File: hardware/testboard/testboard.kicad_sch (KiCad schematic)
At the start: 0 parts

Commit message: work on testboard, move 3d models
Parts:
- added C19: 100nF, symbol Device:C
- added U5: 74LVC1G04, symbol 74xGxx:74LVC1G04
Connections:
- new net +5V: C19.1, U5.5 (VCC)
- new net GND: C19.2, U5.3 (GND)
- new net R/~{W}: U5.2
- new net ~{R}/W: U5.4
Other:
- added sheet Clock (clock.kicad_sch)
- added sheet FPGA (fpga.kicad_sch)
- added sheet IO (io.kicad_sch)
- added sheet Power (power.kicad_sch)
- added sheet Resizer (resizer.kicad_sch)
- added sheet SRAM (sram.kicad_sch)
- sheet CPU ports: added A[0..31], BCLK, D[0..31], PCLK, R/~{W}, SIZ[0..1], TM[0..2], TT[0..1], ~{AVEC}, ~{IPL[0..2]}, ~{RSTI}, ~{RSTO}, ~{TA}, ~{TCI}/~{TBI}, ~{TEA}, ~{TIP}, ~{TS}; removed none

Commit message: work on testboard
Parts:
- removed C19: 100nF, symbol Device:C
- removed U5: 74LVC1G04, symbol 74xGxx:74LVC1G04
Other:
- sheet CPU ports: added ~{R}/W, ~{TBI}, ~{TCI}; removed ~{TCI}/~{TBI}

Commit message: root mostly finished
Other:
- sheet FPGA ports: added D[0..31], IPL[0..2], R/~{W}, SIZ[0..1], TM[0..2], TT[0..1], ~{COM_IACK}, ~{COM_IRQ}, ~{TA}, ~{TBI}, ~{TCI}, ~{TEA}, ~{TIP}, ~{TS}; removed PA[0..1], PD[24..31]

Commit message: work on testboard
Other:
- sheet FPGA ports: added ~{IPL[0..2]}; removed IPL[0..2]
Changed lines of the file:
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@@
-      (effects (font (size 1.27 1.27)) (justify left))
-    )
-    (pin "IPL[0..2]" output (at 137.16 96.52 180)
       (effects (font (size 1.27 1.27)) (justify left))
     )
@@
       (effects (font (size 1.27 1.27)) (justify right))
     )
+    (pin "~{IPL[0..2]}" output (at 137.16 96.52 180)
+      (effects (font (size 1.27 1.27)) (justify left))
+    )
     (instances

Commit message: simpleboard nearly complete
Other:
- added sheet Reset (reset.kicad_sch)
- sheet FPGA ports: added ~{FPGA_RDY}, ~{RST}; removed none
- sheet Power ports: added none; removed PWR_GOOD
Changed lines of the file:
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@@
+    (stroke (width 0) (type default))
+  )
+  (wire (pts (xy 124.46 124.46) (xy 137.16 124.46))
     (stroke (width 0) (type default))
   )
@@
     (stroke (width 0) (type default))
   )
+  (wire (pts (xy 220.98 106.68) (xy 233.68 106.68))
+    (stroke (width 0) (type default))
+  )
   (wire (pts (xy 48.26 142.24) (xy 58.42 142.24))
     (stroke (width 0) (type default))
   )
+  (wire (pts (xy 124.46 45.72) (xy 137.16 45.72))
+    (stroke (width 0) (type default))
+  )
   (wire (pts (xy 83.82 121.92) (xy 96.52 121.92))
     (stroke (width 0) (type default))
@@
     (stroke (width 0) (type default))
   )
+  (wire (pts (xy 91.44 30.48) (xy 101.6 30.48))
+    (stroke (width 0) (type default))
+  )
   (bus (pts (xy 124.46 88.9) (xy 137.16 88.9))
     (stroke (width 0) (type default))
@@
     (stroke (width 0) (type default))
   )
+  (wire (pts (xy 91.44 27.94) (xy 101.6 27.94))
+    (stroke (width 0) (type default))
+  )
   (wire (pts (xy 27.94 25.4) (xy 38.1 25.4))
     (stroke (width 0) (type default))
@@
     (stroke (width 0) (type default))
   )
+  (wire (pts (xy 48.26 162.56) (xy 60.96 162.56))
+    (stroke (width 0) (type default))
+  )
   (bus (pts (xy 101.6 22.86) (xy 91.44 22.86))
     (stroke (width 0) (type default))
@@
     (stroke (width 0) (type default))
   )
+  (wire (pts (xy 60.96 160.02) (xy 48.26 160.02))
+    (stroke (width 0) (type default))
+  )
   (bus (pts (xy 101.6 45.72) (xy 91.44 45.72))
     (stroke (width 0) (type default))
@@
     (stroke (width 0) (type default))
   )
+  (wire (pts (xy 96.52 160.02) (xy 83.82 160.02))
+    (stroke (width 0) (type default))
+  )
   (wire (pts (xy 91.44 83.82) (xy 101.6 83.82))
     (stroke (width 0) (type default))
@@
     (effects (font (size 1.27 1.27)) (justify right bottom))
   )
+  (label "~{SW_RST}" (at 101.6 30.48 180) (fields_autoplaced)
+    (effects (font (size 1.27 1.27)) (justify right bottom))
+  )
   (label "~{AVEC}" (at 101.6 83.82 180) (fields_autoplaced)
     (effects (font (size 1.27 1.27)) (justify right bottom))
   )
+  (label "~{FPGA_RDY}" (at 124.46 124.46 0) (fields_autoplaced)
+    (effects (font (size 1.27 1.27)) (justify left bottom))
+  )
   (label "~{DSACK[0..1]}" (at 96.52 129.54 180) (fields_autoplaced)
     (effects (font (size 1.27 1.27)) (justify right bottom))
@@
     (effects (font (size 1.27 1.27)) (justify right bottom))
   )
+  (label "~{RST}" (at 101.6 27.94 180) (fields_autoplaced)
+    (effects (font (size 1.27 1.27)) (justify right bottom))
+  )
+  (label "~{SW_RST}" (at 48.26 160.02 0) (fields_autoplaced)
+    (effects (font (size 1.27 1.27)) (justify left bottom))
+  )
   (label "~{RAM_CS}" (at 200.66 53.34 180) (fields_autoplaced)
     (effects (font (size 1.27 1.27)) (justify right bottom))
@@
     (effects (font (size 1.27 1.27)) (justify left bottom))
   )
+  (label "~{RST}" (at 124.46 45.72 0) (fields_autoplaced)
+    (effects (font (size 1.27 1.27)) (justify left bottom))
+  )
   (label "~{SWE}" (at 220.98 119.38 0) (fields_autoplaced)
     (effects (font (size 1.27 1.27)) (justify left bottom))
@@
     (effects (font (size 1.27 1.27)) (justify right bottom))
   )
+  (label "~{RST}" (at 96.52 160.02 180) (fields_autoplaced)
+    (effects (font (size 1.27 1.27)) (justify right bottom))
+  )
   (label "PA[0..1]" (at 96.52 111.76 180) (fields_autoplaced)
     (effects (font (size 1.27 1.27)) (justify right bottom))
@@
     (effects (font (size 1.27 1.27)) (justify right bottom))
   )
+  (label "~{RST}" (at 220.98 106.68 0) (fields_autoplaced)
+    (effects (font (size 1.27 1.27)) (justify left bottom))
+  )
   (label "TM[0..2]" (at 124.46 93.98 0) (fields_autoplaced)
     (effects (font (size 1.27 1.27)) (justify left bottom))
@@
   )
   (label "A[2..19]" (at 220.98 43.18 0) (fields_autoplaced)
+    (effects (font (size 1.27 1.27)) (justify left bottom))
+  )
+  (label "~{FPGA_RDY}" (at 48.26 162.56 0) (fields_autoplaced)
     (effects (font (size 1.27 1.27)) (justify left bottom))
   )
@@
     )
   )
-  (sheet (at 119.38 154.94) (size 27.94 25.4) (fields_autoplaced)
+  (sheet (at 22.86 180.34) (size 17.78 7.62) (fields_autoplaced)
     (stroke (width 0.1524) (type solid))
     (fill (color 0 0 0 0.0000))
-    (property "Sheetname" "Power" (at 119.38 154.2284 0)
+    (property "Sheetname" "Power" (at 22.86 179.6284 0)
       (effects (font (size 1.27 1.27)) (justify left bottom))
     )
-    (property "Sheetfile" "power.kicad_sch" (at 119.38 180.9246 0)
+    (property "Sheetfile" "power.kicad_sch" (at 22.86 188.5446 0)
       (effects (font (size 1.27 1.27)) (justify left top))
-    )
-    (pin "PWR_GOOD" output (at 147.32 175.26 0)
-      (effects (font (size 1.27 1.27)) (justify right))
     )
     (instances
@@
     )
   )
-  (sheet (at 137.16 48.26) (size 50.8 73.66) (fields_autoplaced)
+  (sheet (at 137.16 43.18) (size 50.8 83.82) (fields_autoplaced)
     (stroke (width 0.1524) (type solid))
     (fill (color 0 0 0 0.0000))
-    (property "Sheetname" "FPGA" (at 137.16 47.5484 0)
+    (property "Sheetname" "FPGA" (at 137.16 42.4684 0)
       (effects (font (size 1.27 1.27)) (justify left bottom))
     )
-    (property "Sheetfile" "fpga.kicad_sch" (at 137.16 122.5046 0)
+    (property "Sheetfile" "fpga.kicad_sch" (at 137.16 127.5846 0)
       (effects (font (size 1.27 1.27)) (justify left top))
     )
@@
     )
     (pin "~{IPL[0..2]}" output (at 137.16 96.52 180)
+      (effects (font (size 1.27 1.27)) (justify left))
+    )
+    (pin "~{FPGA_RDY}" output (at 137.16 124.46 180)
+      (effects (font (size 1.27 1.27)) (justify left))
+    )
+    (pin "~{RST}" input (at 137.16 45.72 180)
       (effects (font (size 1.27 1.27)) (justify left))
     )
@@
       )
     )
+  )
+  (sheet (at 60.96 157.48) (size 22.86 12.7) (fields_autoplaced)
+    (stroke (width 0.1524) (type solid))
+    (fill (color 0 0 0 0.0000))
+    (property "Sheetname" "Reset" (at 60.96 156.7684 0)
+      (effects (font (size 1.27 1.27)) (justify left bottom))
+    )
+    (property "Sheetfile" "reset.kicad_sch" (at 60.96 170.7646 0)
+      (effects (font (size 1.27 1.27)) (justify left top))
+    )
+    (pin "~{RST}" output (at 83.82 160.02 0)
+      (effects (font (size 1.27 1.27)) (justify right))
+    )
+    (pin "SW_RST" input (at 60.96 160.02 180)
+      (effects (font (size 1.27 1.27)) (justify left))
+    )
+    (pin "~{FPGA_RDY}" input (at 60.96 162.56 180)
+      (effects (font (size 1.27 1.27)) (justify left))
+    )
+    (instances
+      (project "testboard"
+        (path "/a1ce156a-fb78-423b-b05a-d07384e5c8a7" (page "12"))
+      )
+    )

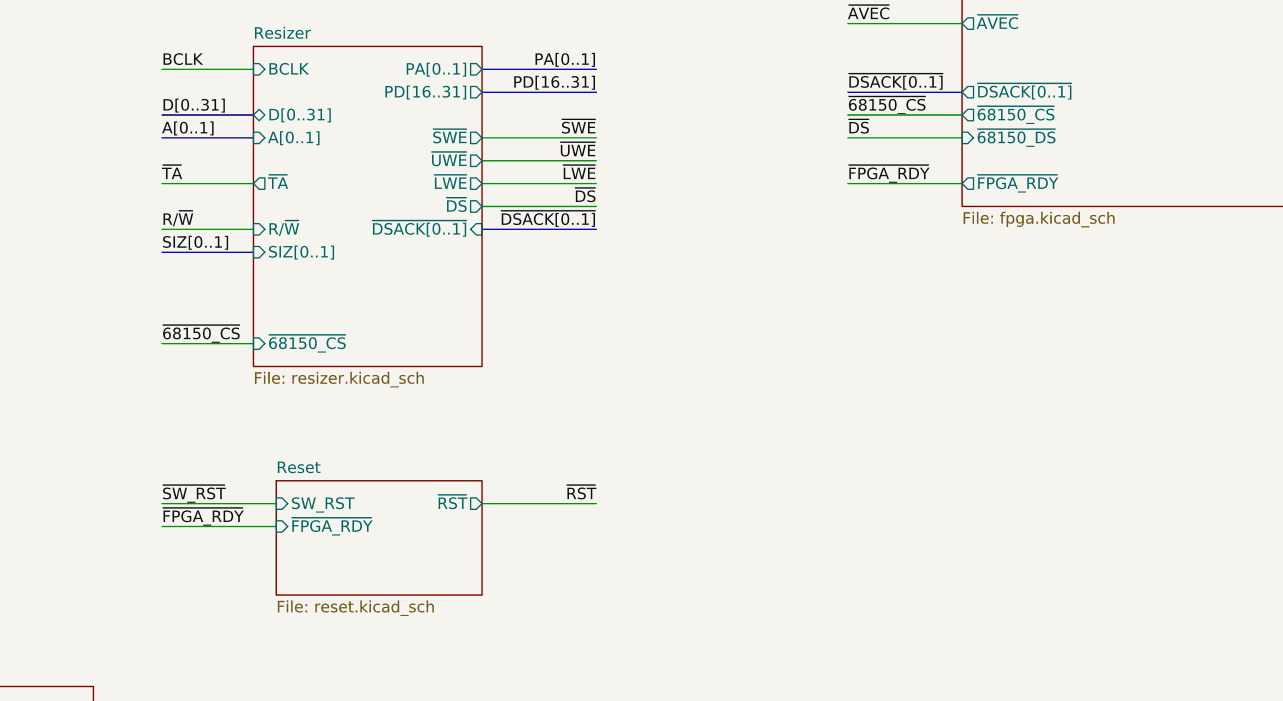
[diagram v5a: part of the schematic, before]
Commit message: testboard - schematic and route done
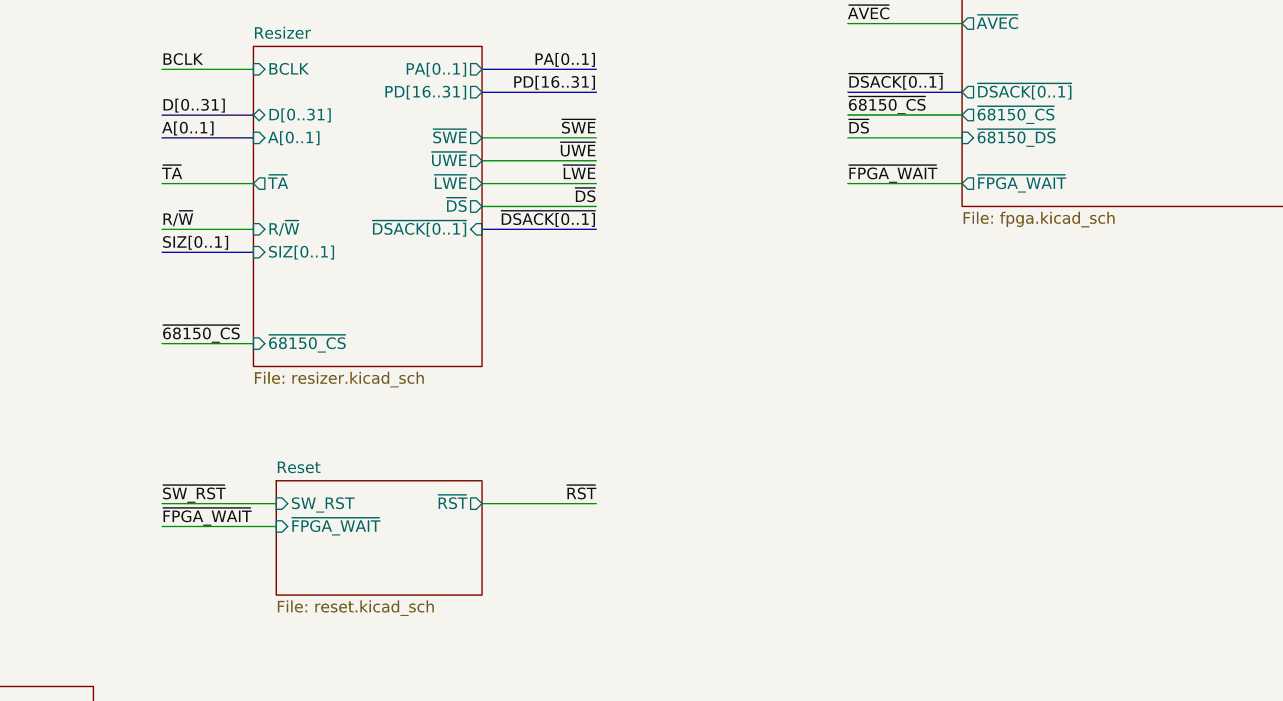
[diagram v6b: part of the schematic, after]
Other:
- sheet FPGA ports: added ~{FPGA_WAIT}; removed ~{FPGA_RDY}
- sheet Reset ports: added ~{FPGA_WAIT}; removed ~{FPGA_RDY}
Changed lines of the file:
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@@
     (effects (font (size 1.27 1.27)) (justify right bottom))
   )
-  (label "~{FPGA_RDY}" (at 124.46 124.46 0) (fields_autoplaced)
+  (label "~{FPGA_WAIT}" (at 124.46 124.46 0) (fields_autoplaced)
     (effects (font (size 1.27 1.27)) (justify left bottom))
   )
@@
     (effects (font (size 1.27 1.27)) (justify left bottom))
   )
-  (label "~{FPGA_RDY}" (at 48.26 162.56 0) (fields_autoplaced)
+  (label "~{FPGA_WAIT}" (at 48.26 162.56 0) (fields_autoplaced)
     (effects (font (size 1.27 1.27)) (justify left bottom))
   )
@@
       (effects (font (size 1.27 1.27)) (justify left))
     )
-    (pin "~{FPGA_RDY}" output (at 137.16 124.46 180)
+    (pin "~{FPGA_WAIT}" output (at 137.16 124.46 180)
       (effects (font (size 1.27 1.27)) (justify left))
     )
@@
       (effects (font (size 1.27 1.27)) (justify left))
     )
-    (pin "~{FPGA_RDY}" input (at 60.96 162.56 180)
-      (effects (font (size 1.27 1.27)) (justify left))
-    )
+    (pin "~{FPGA_WAIT}" input (at 60.96 162.56 180)
+      (effects (font (size 1.27 1.27)) (justify left))
+    )

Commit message: Gerbers published, board out for production!
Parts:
- added H1, H2, H3: MountingHole, MountingHole:MountingHole_3.2mm_M3, symbol Mechanical:MountingHole
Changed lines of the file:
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@@
     (effects (font (size 1.27 1.27)) (justify left bottom))
+  )
+  (symbol (lib_id "Mechanical:MountingHole") (at 142.24 180.34 0) (unit 1)
+    (in_bom yes) (on_board yes) (dnp no) (fields_autoplaced)
+    (property "Reference" "H2" (at 144.78 179.07 0)
+      (effects (font (size 1.27 1.27)) (justify left))
+    )
+    (property "Value" "MountingHole" (at 144.78 181.61 0)
+      (effects (font (size 1.27 1.27)) (justify left))
+    )
+    (property "Footprint" "MountingHole:MountingHole_3.2mm_M3" (at 142.24 180.34 0)
+      (effects (font (size 1.27 1.27)) hide)
+    )
+    (property "Datasheet" "~" (at 142.24 180.34 0)
+      (effects (font (size 1.27 1.27)) hide)
+    )
+    (instances
+      (project "testboard"
+        (path "/a1ce156a-fb78-423b-b05a-d07384e5c8a7"
+          (reference "H2") (unit 1)
+        )
+      )
+    )
+  )
+  (symbol (lib_id "Mechanical:MountingHole") (at 142.24 175.26 0) (unit 1)
+    (in_bom yes) (on_board yes) (dnp no) (fields_autoplaced)
+    (property "Reference" "H1" (at 144.78 173.99 0)
+      (effects (font (size 1.27 1.27)) (justify left))
+    )
+    (property "Value" "MountingHole" (at 144.78 176.53 0)
+      (effects (font (size 1.27 1.27)) (justify left))
+    )
+    (property "Footprint" "MountingHole:MountingHole_3.2mm_M3" (at 142.24 175.26 0)
+      (effects (font (size 1.27 1.27)) hide)
+    )
+    (property "Datasheet" "~" (at 142.24 175.26 0)
+      (effects (font (size 1.27 1.27)) hide)
+    )
+    (instances
+      (project "testboard"
+        (path "/a1ce156a-fb78-423b-b05a-d07384e5c8a7"
+          (reference "H1") (unit 1)
+        )
+      )
+    )
+  )
+  (symbol (lib_id "Mechanical:MountingHole") (at 142.24 185.42 0) (unit 1)
+    (in_bom yes) (on_board yes) (dnp no) (fields_autoplaced)
+    (property "Reference" "H3" (at 144.78 184.15 0)
+      (effects (font (size 1.27 1.27)) (justify left))
+    )
+    (property "Value" "MountingHole" (at 144.78 186.69 0)
+      (effects (font (size 1.27 1.27)) (justify left))
+    )
+    (property "Footprint" "MountingHole:MountingHole_3.2mm_M3" (at 142.24 185.42 0)
+      (effects (font (size 1.27 1.27)) hide)
+    )
+    (property "Datasheet" "~" (at 142.24 185.42 0)
+      (effects (font (size 1.27 1.27)) hide)
+    )
+    (instances
+      (project "testboard"
+        (path "/a1ce156a-fb78-423b-b05a-d07384e5c8a7"
+          (reference "H3") (unit 1)
+        )
+      )
+    )
   )
   (sheet (at 233.68 104.14) (size 30.48 30.48) (fields_autoplaced)
